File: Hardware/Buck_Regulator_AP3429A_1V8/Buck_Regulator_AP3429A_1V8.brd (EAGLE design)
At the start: 25.4 x 25.4 mm, 51 parts, among them J1 Screw Terminal, J2 POWER_JACKPOWER_JACK_SLOT_COM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, J3 Breakout Headers, U1 AP3429/A

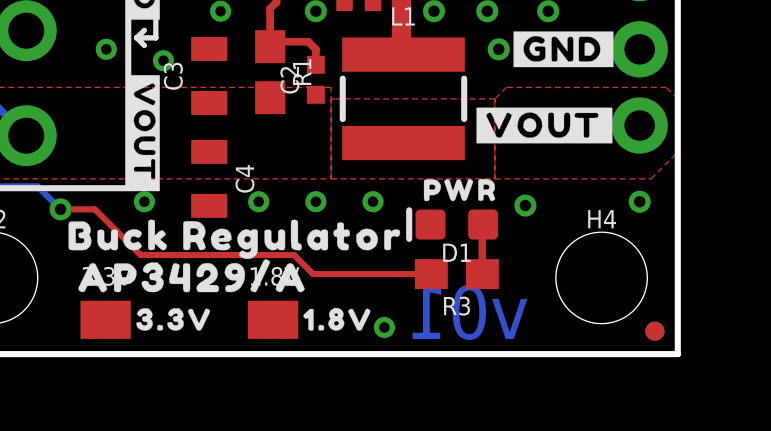
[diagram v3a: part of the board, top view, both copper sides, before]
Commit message: Updated files for design review
Changed the version number on the board file to be V10 instead of V01, then changed the footprint of the power jack on each side of the board to swap the sides of the exposed copper on the groundbreak pins for easier soldering.
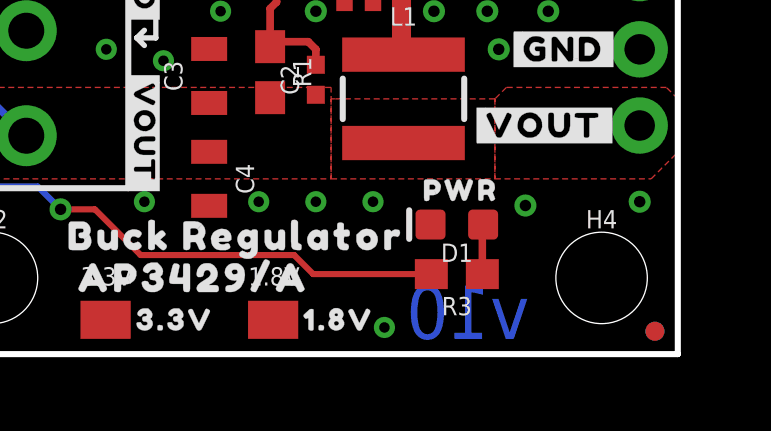
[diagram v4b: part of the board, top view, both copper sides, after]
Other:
- board text added: "v10"
- board text removed: "v01"
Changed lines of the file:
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@@
 <drawing>
 <settings>
-<setting alwaysvectorfont="no"/>
+<setting alwaysvectorfont="yes"/>
 <setting verticaltext="up"/>
 </settings>
@@
 <layer number="28" name="bValues" color="7" fill="1" visible="no" active="yes"/>
 <layer number="29" name="tStop" color="7" fill="3" visible="no" active="yes"/>
-<layer number="30" name="bStop" color="7" fill="6" visible="yes" active="yes"/>
+<layer number="30" name="bStop" color="7" fill="6" visible="no" active="yes"/>
 <layer number="31" name="tCream" color="7" fill="4" visible="no" active="yes"/>
 <layer number="32" name="bCream" color="7" fill="5" visible="no" active="yes"/>
@@
 <layer number="45" name="Holes" color="7" fill="1" visible="yes" active="yes"/>
 <layer number="46" name="Milling" color="3" fill="1" visible="no" active="yes"/>
-<layer number="47" name="Measures" color="7" fill="1" visible="yes" active="yes"/>
+<layer number="47" name="Measures" color="7" fill="1" visible="no" active="yes"/>
 <layer number="48" name="Document" color="7" fill="1" visible="no" active="yes"/>
 <layer number="49" name="Reference" color="7" fill="1" visible="no" active="yes"/>
@@
 <wire x1="7.366" y1="10.541" x2="7.62" y2="10.795" width="0.1778" layer="21"/>
 <wire x1="7.366" y1="10.541" x2="7.62" y2="10.287" width="0.1778" layer="21"/>
-<text x="20.447" y="0.508" size="1.778" layer="16" font="vector" ratio="15" rot="MR0">v01</text>
+<text x="20.447" y="0.508" size="1.778" layer="16" font="vector" ratio="15" rot="MR0">v10</text>
 <text x="16.51" y="-44.45" size="1.778" layer="51" font="vector" ratio="10" distance="15">M. Chodikov</text>
 <wire x1="5.334" y1="11.176" x2="5.334" y2="10.414" width="0.2032" layer="22"/>
@@
 <attribute name="VALUE" x="8.89" y="5.842" size="0.6096" layer="27" font="vector" ratio="20" rot="R270" align="top-center"/>
 </element>
+<element name="U$16" library="output" package="BUCK_REGULATOR_AP3429#A3453" value="" x="1.524" y="12.827" smashed="yes" rot="MR90"/>
 <element name="J2" library="SparkFun-Connectors" package="POWER_JACK_PTH_SLOT_BOTH" value="POWER_JACKPOWER_JACK_SLOT_COMBO" x="13.335" y="24.003" smashed="yes" rot="R90"/>
-<element name="U$16" library="output" package="BUCK_REGULATOR_AP3429#A3453" value="" x="1.524" y="12.827" smashed="yes" rot="MR90"/>
 </elements>
 <signals>
@@
 <contactref element="J1" pad="1"/>
 <contactref element="C1" pad="1"/>
-<contactref element="J2" pad="PWR"/>
 <polygon width="0.2032" layer="1" isolate="0.3048">
 <vertex x="2.159" y="18.923"/>
@@
 <vertex x="2.667" y="19.431"/>
 </polygon>
+<contactref element="J2" pad="PWR"/>
 </signal>
 <signal name="GND">
@@
 <contactref element="C3" pad="2"/>
 <contactref element="C4" pad="2"/>
-<contactref element="J2" pad="GND"/>
 <polygon width="0.2032" layer="1" isolate="0.3048" rank="2">
 <vertex x="0" y="0"/>
@@
 <via x="16.51" y="24.13" extent="1-16" drill="0.35"/>
 <via x="10.16" y="24.13" extent="1-16" drill="0.35"/>
+<contactref element="J2" pad="GND"/>
 </signal>
 <signal name="N$1">
@@
 </signals>
 <mfgpreviewcolors>
-<mfgpreviewcolor name="soldermaskcolor" color="0xC8000000"/>
-<mfgpreviewcolor name="silkscreencolor" color="0xFFFEFEFE"/>
+<mfgpreviewcolor name="soldermaskcolor" color="0xC8FF0000"/>
+<mfgpreviewcolor name="silkscreencolor" color="0xFFFFFFFF"/>
 <mfgpreviewcolor name="backgroundcolor" color="0xFF282828"/>
 <mfgpreviewcolor name="coppercolor" color="0xFFFFBF00"/>

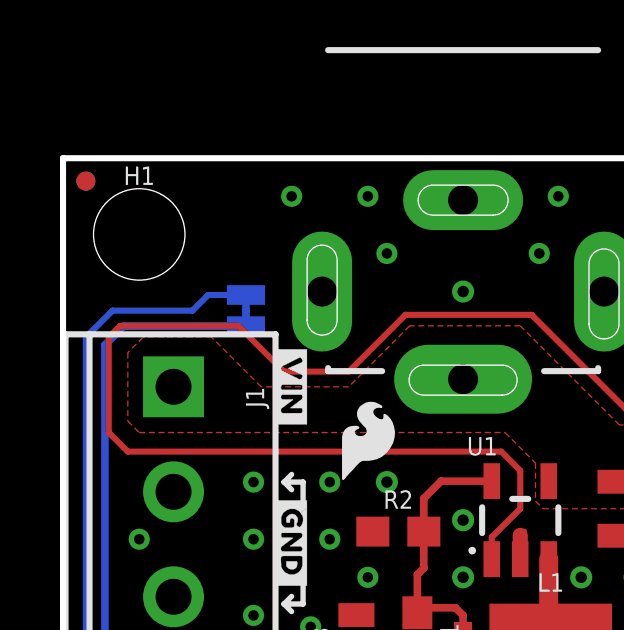
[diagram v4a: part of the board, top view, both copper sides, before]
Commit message: Changed version number in schematic, adjusted components
Moved around some silkscreen in order for easier reading on the backside; changed the version number in the schematic to v10
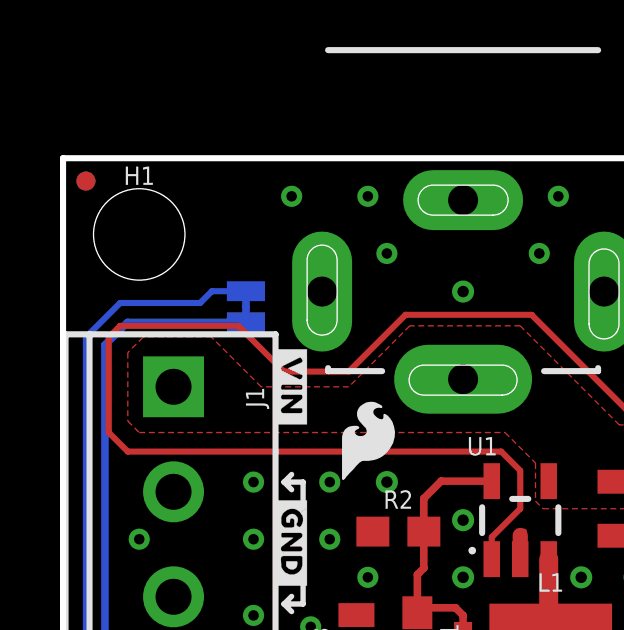
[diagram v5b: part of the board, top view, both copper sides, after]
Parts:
- moved PWR 0.13 mm to (6.10, 20.4)
- moved U$14 0.13 mm to (6.10, 23.2)
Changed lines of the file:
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@@
 <drawing>
 <settings>
-<setting alwaysvectorfont="yes"/>
+<setting alwaysvectorfont="no"/>
 <setting verticaltext="up"/>
 </settings>
@@
 <element name="FRAME1" library="SparkFun-Aesthetics" package="CREATIVE_COMMONS" value="FRAME-LEDGER" x="-10.16" y="-44.45" smashed="yes">
 <attribute name="DESIGNER" value="M. Chodikov" x="69.85" y="-57.15" size="1.778" layer="27" display="off"/>
-<attribute name="REV" value="v01" x="69.85" y="-57.15" size="1.778" layer="27" display="off"/>
+<attribute name="REV" value="v10" x="69.85" y="-57.15" size="1.778" layer="27" display="off"/>
 </element>
 <element name="L1" library="SparkFun-Coils" package="INDUCTOR_4X4MM" value="2.2μH" x="16.256" y="8.509" smashed="yes">
@@
 <attribute name="PROD_ID" value="NDUC-13770" x="48.006" y="-15.621" size="1.778" layer="27" display="off"/>
 </element>
-<element name="PWR" library="SparkFun-Jumpers" package="SMT-JUMPER_2_NC_TRACE_SILK" package3d_urn="urn:adsk.eagle:package:39281/1" value="JUMPER-SMT_2_NC_TRACE_SILK" x="6.096" y="20.32" smashed="yes" rot="MR270">
-<attribute name="NAME" x="4.953" y="20.32" size="0.6096" layer="26" font="vector" ratio="20" rot="MR270" align="bottom-center"/>
+<element name="PWR" library="SparkFun-Jumpers" package="SMT-JUMPER_2_NC_TRACE_SILK" package3d_urn="urn:adsk.eagle:package:39281/1" value="JUMPER-SMT_2_NC_TRACE_SILK" x="6.096" y="20.447" smashed="yes" rot="MR270">
+<attribute name="NAME" x="4.953" y="20.447" size="0.6096" layer="26" font="vector" ratio="20" rot="MR270" align="bottom-center"/>
 </element>
 <element name="R1" library="SparkFun-Resistors" package="0603" value="300k" x="11.811" y="9.398" smashed="yes" rot="R270">
@@
 <element name="U$13" library="output" package="#VOUT#3447" value="" x="5.334" y="7.112" smashed="yes" rot="MR90"/>
 <element name="U$15" library="output" package="#VIN#3445" value="" x="5.334" y="17.78" smashed="yes" rot="MR90"/>
-<element name="U$14" library="output" package="#PWR#3451" value="" x="6.096" y="23.114" smashed="yes" rot="MR90"/>
+<element name="U$14" library="output" package="#PWR#3451" value="" x="6.096" y="23.241" smashed="yes" rot="MR90"/>
 <element name="C1" library="SparkFun-Capacitors" package="0805" value="22uF" x="18.415" y="13.716" smashed="yes" rot="R270">
 <attribute name="NAME" x="19.304" y="13.716" size="0.6096" layer="25" font="vector" ratio="20" rot="R270" align="bottom-center"/>
@@
 <contactref element="PWR" pad="1"/>
 <contactref element="R3" pad="2"/>
-<wire x1="6.096" y1="20.8407" x2="4.8387" y2="20.8407" width="0.2032" layer="16"/>
-<wire x1="1.651" y1="20.32" x2="0.762" y2="19.431" width="0.2032" layer="16"/>
-<wire x1="4.8387" y1="20.8407" x2="4.318" y2="20.32" width="0.2032" layer="16"/>
-<wire x1="4.318" y1="20.32" x2="1.651" y2="20.32" width="0.2032" layer="16"/>
+<wire x1="6.096" y1="20.9677" x2="4.9657" y2="20.9677" width="0.2032" layer="16"/>
+<wire x1="1.905" y1="20.574" x2="0.762" y2="19.431" width="0.2032" layer="16"/>
+<wire x1="4.9657" y1="20.9677" x2="4.572" y2="20.574" width="0.2032" layer="16"/>
+<wire x1="4.572" y1="20.574" x2="1.905" y2="20.574" width="0.2032" layer="16"/>
 <wire x1="13.247" y1="2.667" x2="17.184" y2="2.667" width="0.2032" layer="1"/>
 <wire x1="13.247" y1="2.667" x2="12.612" y2="3.302" width="0.2032" layer="1"/>
@@
 <contactref element="PWR" pad="2"/>
 <wire x1="1.397" y1="19.177" x2="1.397" y2="9.566" width="0.254" layer="16"/>
-<wire x1="6.096" y1="19.7993" x2="2.0193" y2="19.7993" width="0.254" layer="16"/>
-<wire x1="2.0193" y1="19.7993" x2="1.397" y2="19.177" width="0.254" layer="16"/>
+<wire x1="6.096" y1="19.9263" x2="2.1463" y2="19.9263" width="0.254" layer="16"/>
+<wire x1="2.1463" y1="19.9263" x2="1.397" y2="19.177" width="0.254" layer="16"/>
 <contactref element="L1" pad="P$2"/>
 <contactref element="R1" pad="2"/>
